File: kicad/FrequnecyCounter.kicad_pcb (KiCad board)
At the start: 4 copper layers, 130 x 90 mm, 134 parts, among them J1 USB_B, J2 CONN_COAXIAL, J3 CONN_COAXIAL, J4 CONN_COAXIAL, SW1 SW_Push, T1 WBC16-1T, U1 TPS650250, U10 MC12093, U11 tx176, U12 TLV3501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

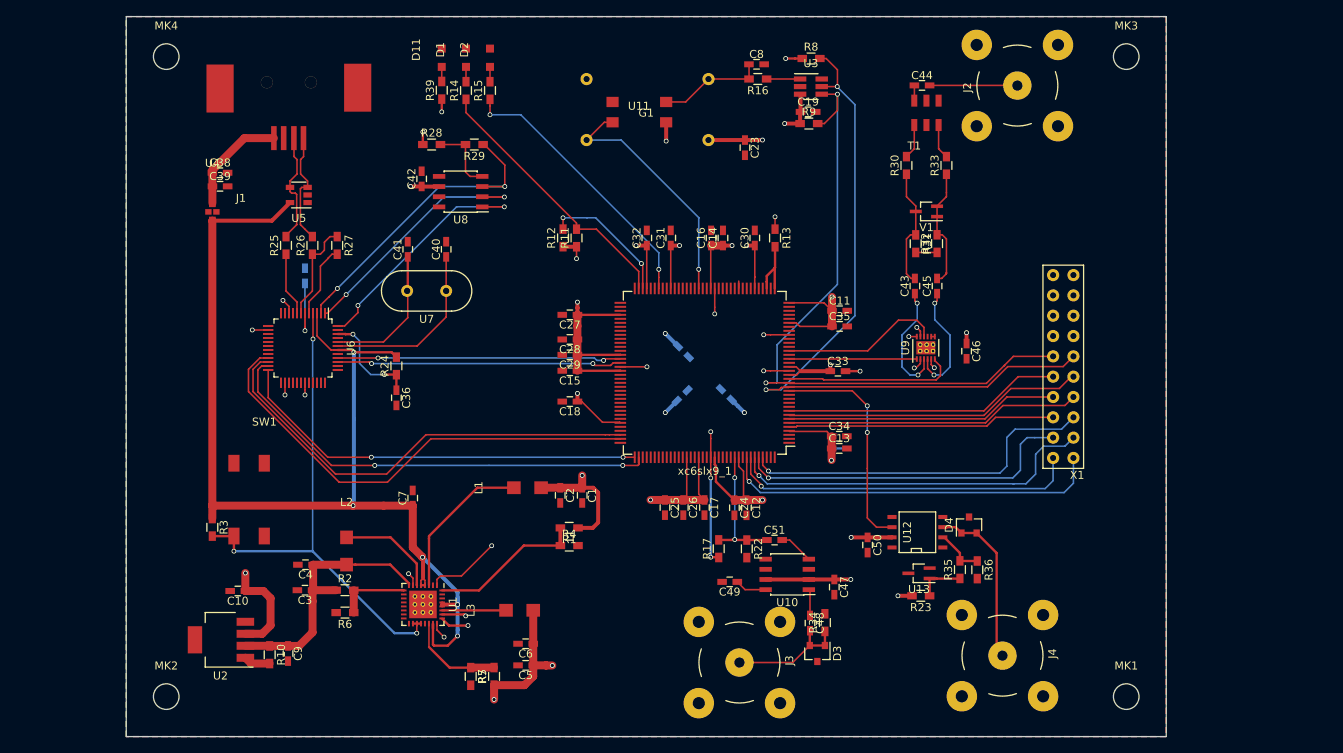
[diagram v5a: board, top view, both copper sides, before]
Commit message: Remove design errors and changes some footprints [to review]
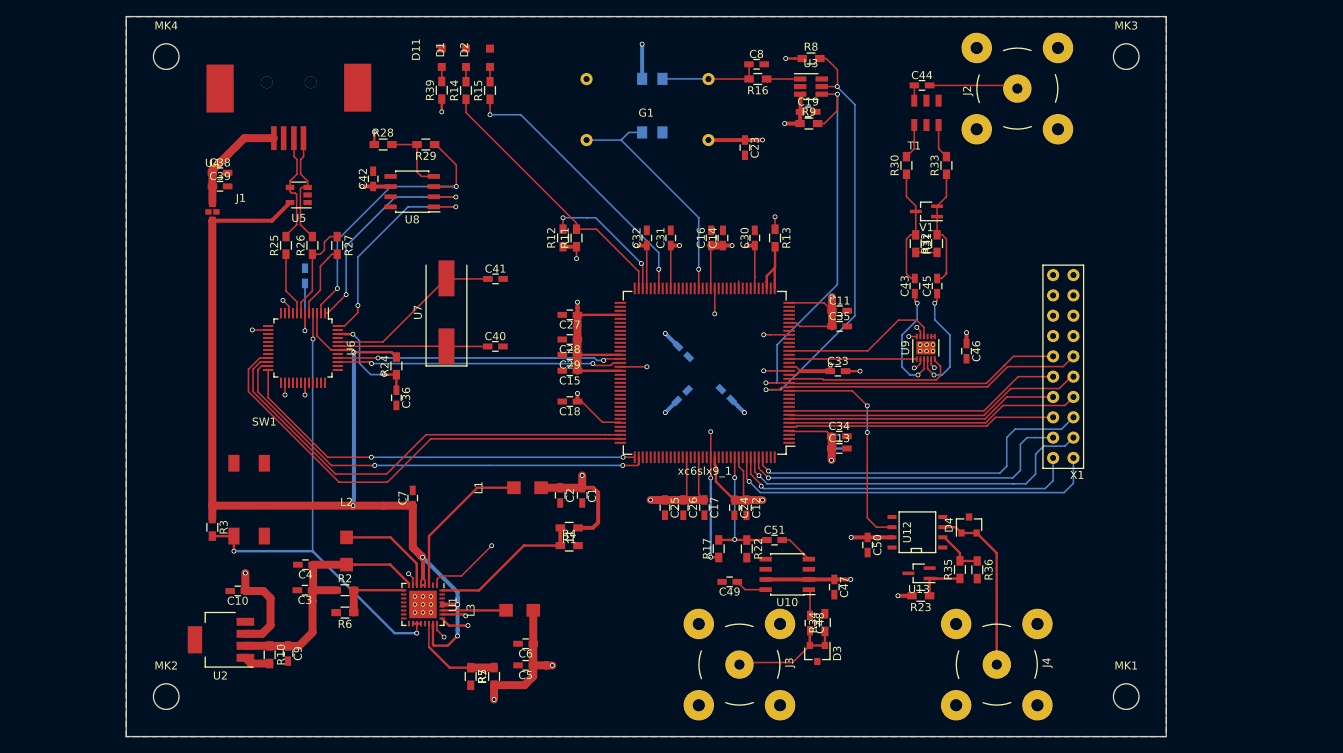
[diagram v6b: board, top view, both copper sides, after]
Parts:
- U11: moved to B.Cu
- U7: footprint Crystals:Crystal_HC49-U_Vertical -> Crystals:Crystal_SMD_HC49-SD
- moved C40 13.6 mm to (116.1, 97.2), turned to 0 degrees
- moved C41 11.6 mm to (116.2, 88.8), turned to 0 degrees
- moved C42 6.06 mm to (100.9, 76.3)
- moved R28 6.06 mm to (102.1, 72.0)
- moved R29 6.06 mm to (107.4, 72.0)
- moved U8 6.06 mm to (105.7, 77.9)
- moved U7 2.68 mm to (110.0, 93.0), turned to 90 degrees
- moved U11 1.91 mm to (138.3, 63.6), turned to 270 degrees
- moved J4 1.33 mm to (178.8, 137.0)
- moved J2 0.38 mm to (181.4, 65.0)
- moved J3 0.26 mm to (146.7, 137.0)
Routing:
- net Net-(C41-Pad1): track 17.6 -> 22.1 mm
- net Net-(C40-Pad1): track 22.6 -> 18.8 mm
- net Net-(U6-Pad48): track 30.8 -> 28.3 mm
- net Net-(U6-Pad1): track 31.7 -> 29.2 mm
- net Net-(R29-Pad1): track 39.4 -> 36.9 mm
- net +3V3: track 65.1 -> 67.1 mm
- net Int_Ref_Clk: track 31.1 -> 29.9 mm
- net /Signal_Input/CH_B: track 21.2 -> 22.0 mm
- net Net-(C8-Pad1): track 13.4 -> 12.7 mm

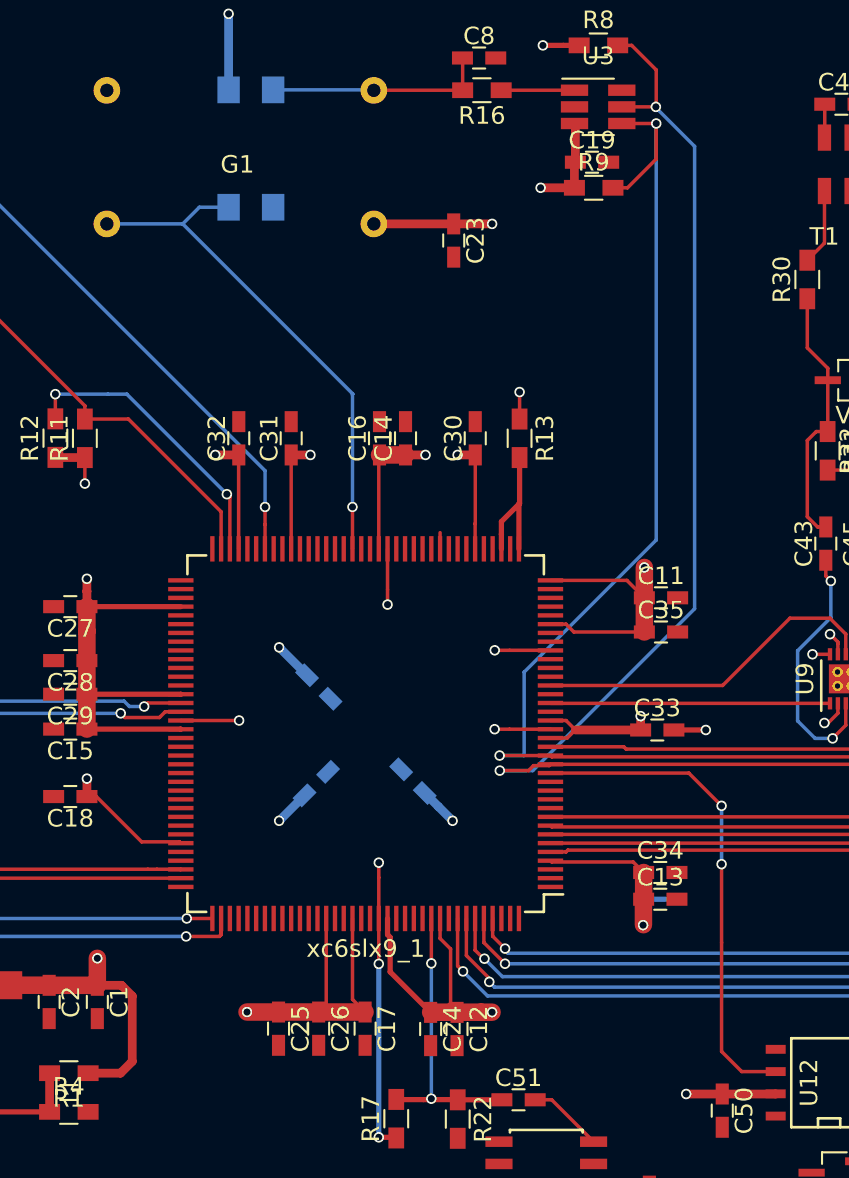
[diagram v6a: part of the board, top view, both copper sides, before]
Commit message: swaping power-plane layer with ground layer [to review]
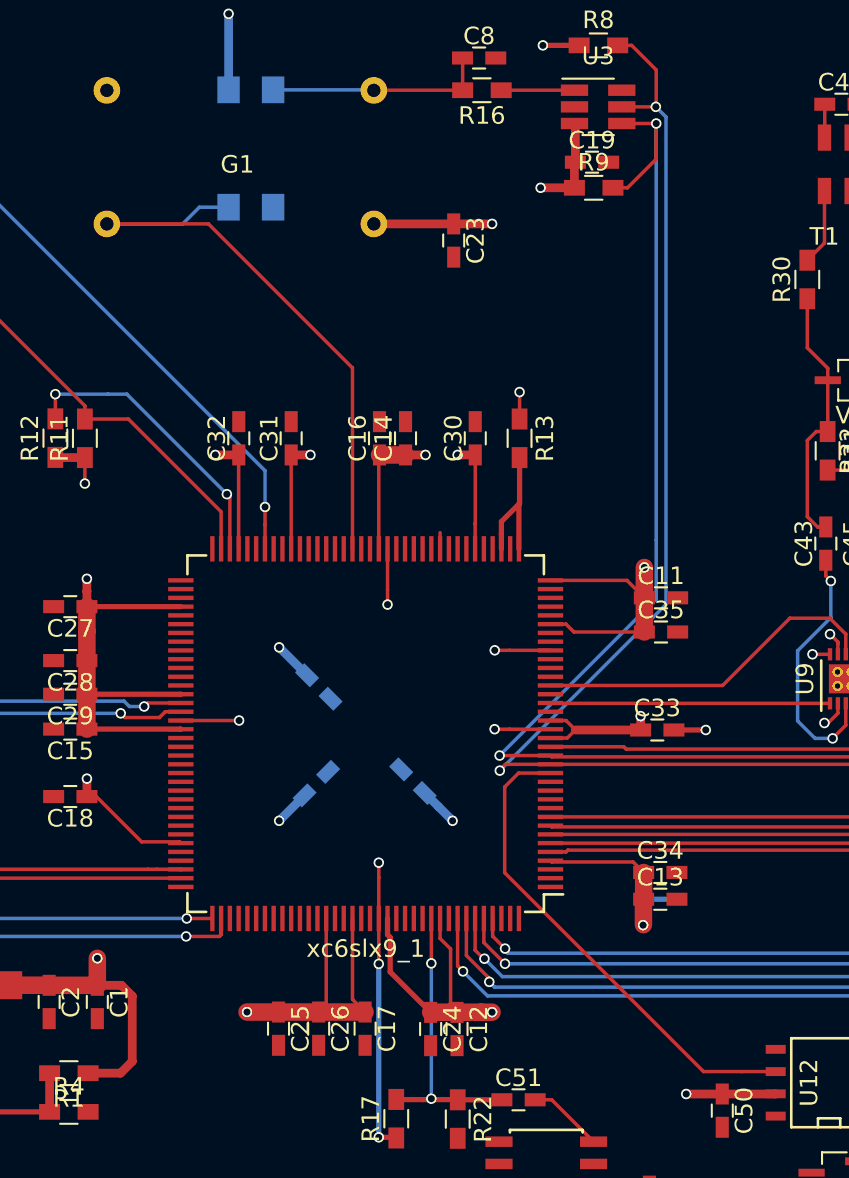
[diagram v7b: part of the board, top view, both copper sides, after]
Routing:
- net Int_Ref_Clk: track 29.9 -> 35.1 mm, vias 1 -> 0
- net (no net): track 744.6 -> 740.2 mm
- net SCL_DAC: track 91.5 -> 89.1 mm
- net SDA_DAC: track 85.7 -> 84.9 mm
- net /FPGA/Clk_B: track 28.1 -> 28.0 mm, vias 2 -> 0
- added copper zone on In2.Cu, net +1.2V
- added copper zone on In2.Cu, net +3V3
- added copper zone on In2.Cu, net +3V3_FPGA
- added copper zone on In1.Cu, net GND
- removed copper zone on In1.Cu, net +1.2V
- removed copper zone on In1.Cu, net +3V3
- removed copper zone on In1.Cu, net +3V3_FPGA
- removed copper zone on In2.Cu, net GND

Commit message: some small schematic and layout changes [completed]
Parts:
- removed D4: BAV99, TO_SOT_Packages_SMD:SOT-23
- removed R12, R13: 4.7k, Resistors_SMD:R_0603_HandSoldering
- removed R23, R36: 1k, Resistors_SMD:R_0603_HandSoldering
- removed R35: 100k, Resistors_SMD:R_0603_HandSoldering
- removed U13: ADR5040, TO_SOT_Packages_SMD:SOT-323_SC-70_Handsoldering
- added C_I2C_1: 1u, Capacitors_SMD:C_0603_HandSoldering, F.Cu at (157.6, 77.5)
- added C_I2C_2: 1u, Capacitors_SMD:C_0603_HandSoldering, F.Cu at (160.8, 77.5)
- added C_JTAG_1: 1u, Capacitors_SMD:C_0603_HandSoldering, F.Cu at (109.1, 109.9)
- added C_JTAG_2: 1u, Capacitors_SMD:C_0603_HandSoldering, F.Cu at (109.1, 113.3)
- added C_RS2232_1: 1u, Capacitors_SMD:C_0603_HandSoldering, F.Cu at (118.4, 97.2)
- added C_RS2232_2: 1u, Capacitors_SMD:C_0603_HandSoldering, F.Cu at (118.4, 100.7)
- added C_TP_1: 1u, Capacitors_SMD:C_0603_HandSoldering, F.Cu at (167.1, 111.9)
- added C_TP_2: 1u, Capacitors_SMD:C_0603_HandSoldering, F.Cu at (167.1, 116.7)
- added R18: 100R, Resistors_SMD:R_0603_HandSoldering, F.Cu at (155.6, 133.9)
- added R19: 100R, Resistors_SMD:R_0603_HandSoldering, F.Cu at (179.9, 125.4)
- added V2: HSMS-281C-TR1G, TO_SOT_Packages_SMD:SOT-323_SC-70_Handsoldering, F.Cu at (178.1, 121.9)
- moved C41 5.51 mm to (111.7, 85.6)
- moved C40 5.46 mm to (111.7, 94.1)
- moved R24 4.49 mm to (102.0, 103.8), turned to 270 degrees
- moved U7 4.48 mm to (106.9, 89.8)
- moved C48 3.36 mm to (158.3, 130.0)
- moved D3 3.36 mm to (159.2, 133.8)
- moved R34 3.36 mm to (160.2, 130.0)
- moved R1 2.61 mm to (127.9, 119.3)
- moved R4 2.61 mm to (127.9, 121.5)
- moved C50 2.33 mm to (164.9, 122.8)
- moved U12 2.33 mm to (171.1, 121.2)
- moved C47 1.89 mm to (158.5, 125.4), turned to 90 degrees
- moved C28 1.34 mm to (125.5, 95.0)
- moved C29 1.34 mm to (125.5, 96.9)
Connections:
- J3 pad 1: /Signal_Input/CH_A -> Net-(J3-Pad1)
- J4 pad 1: /Signal_Input/CH_B -> Net-(J4-Pad1)
- R3 pad 2: /Power_Supply/~RESET -> /FPGA/~RESET
- SW1 pad 1: /Power_Supply/~RESET -> /FPGA/~RESET
- U1 pad 18: /Power_Supply/~RESET -> /FPGA/~RESET
- U1 pad 19: /Power_Supply/~RESET -> /FPGA/~RESET
- U1 pad 20: /Power_Supply/~RESET -> /FPGA/~RESET
- U12 pad 2: Net-(R35-Pad2) -> GND
- U12 pad 8: Net-(U12-Pad8) -> GND
- U6 pad 4: /Power_Supply/~RESET -> /FPGA/~RESET
- xc6slx9_1 pad 37: Net-(R13-Pad2) -> /FPGA/~RESET
- xc6slx9_1 pad 39: Net-(R13-Pad2) -> Net-(xc6slx9_1-Pad39)
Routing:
- net /FPGA/~RESET: track 0.00 -> 127.1 mm, vias 0 -> 5
- net /Power_Supply/~RESET: track 63.7 -> 0.00 mm, vias 3 -> 0
- net Net-(xc6slx9_1-Pad70): track 16.8 -> 0.00 mm, vias 2 -> 0
- net (no net): track 740.2 -> 752.2 mm
- net /Signal_Input/CH_B: track 22.0 -> 10.2 mm
- net Net-(J4-Pad1): track 0.00 -> 11.6 mm
- net Net-(J3-Pad1): track 0.00 -> 10.3 mm
- net +3V3: track 67.1 -> 77.3 mm, vias 18 -> 25
- net Net-(R13-Pad2): track 8.26 -> 0.00 mm
- net /Signal_Input/CH_A: track 15.3 -> 8.36 mm
- net Net-(R35-Pad2): track 6.11 -> 0.00 mm
- net Net-(R23-Pad1): track 5.96 -> 0.00 mm
- net +1.2V: track 60.9 -> 56.0 mm, vias 12 -> 14
- net Net-(R1-Pad2): track 19.5 -> 23.2 mm
- net +3V3_FPGA: track 151.6 -> 155.3 mm, vias 16 -> 22
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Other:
- board text added: "+1.2V"
- board text added: "+3.3V"
- board text added: "+3.3V FPGA"
